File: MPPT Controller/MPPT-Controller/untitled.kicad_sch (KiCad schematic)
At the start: 29 parts, among them J5 USB_C_Receptacle_USB2.0_16P, U2 ESP32-WROOM-32D, U3 CH340C

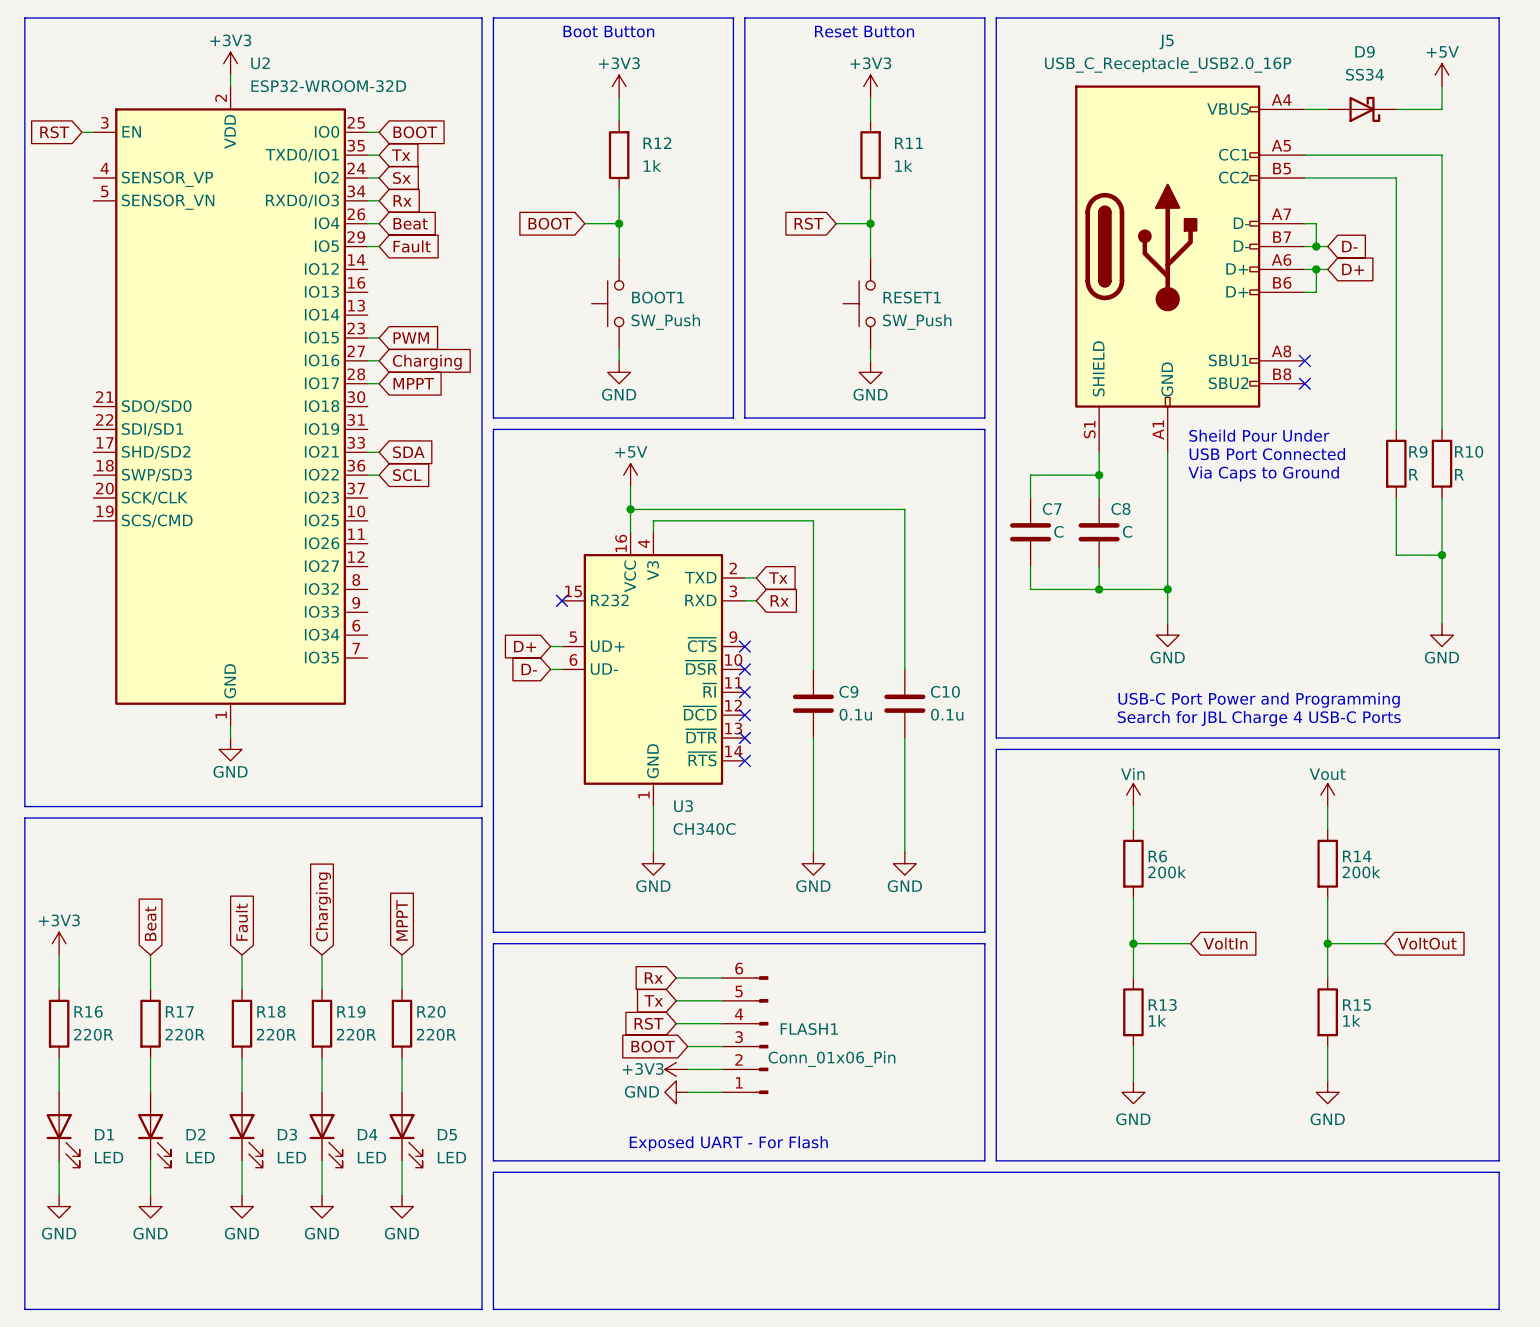
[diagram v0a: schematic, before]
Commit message: Add ADC Channels
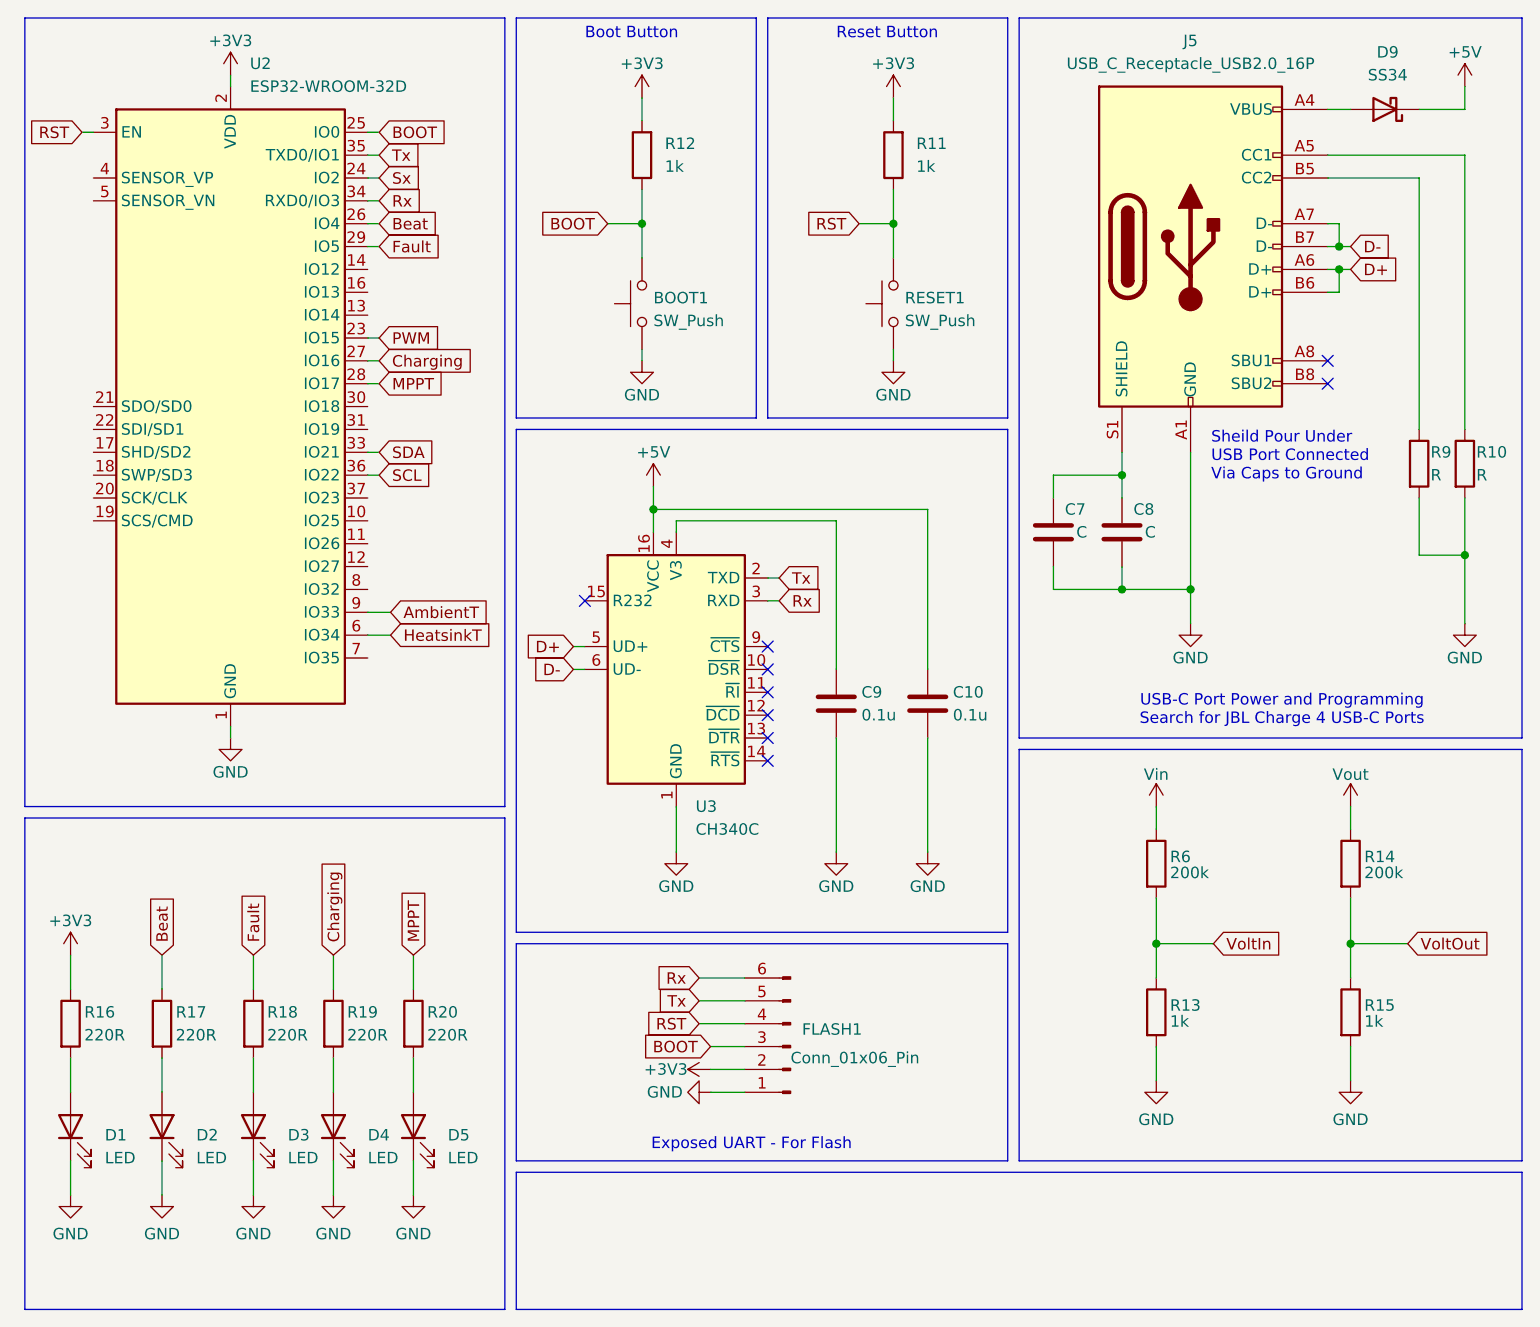
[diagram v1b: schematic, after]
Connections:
- net HeatsinkT: now reaches U2.6 (IO34)
- net AmbientT: now reaches U2.9 (IO33)
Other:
- moved on the sheet: BOOT1, C10, C7, C8, C9, D1, D2, D3, D4, D5, D9, FLASH1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

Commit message: Diode
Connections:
- net RDY1: now reaches U2.30 (IO18)
- net RDY2: now reaches U2.31 (IO19)
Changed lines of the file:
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@@
+	(wire
+		(pts
+			(xy 50.8 58.42) (xy 52.07 58.42)
+		)
+		(stroke
+			(width 0)
+			(type default)
+		)
+	)
 	(wire
 		(pts
@@
 	(wire
 		(pts
+			(xy 50.8 55.88) (xy 52.07 55.88)
+		)
+		(stroke
+			(width 0)
+			(type default)
+		)
+	)
+	(wire
+		(pts
 			(xy 38.1 139.7) (xy 38.1 143.51)
 		)
@@
 		)
 	)
+	(global_label "RDY1"
+		(shape input)
+		(at 52.07 55.88 0)
+		(fields_autoplaced yes)
+		(effects
+			(font
+				(size 1.27 1.27)
+			)
+			(justify left)
+		)
+		(property "Intersheetrefs" "${INTERSHEET_REFS}"
+			(at 59.8933 55.88 0)
+			(effects
+				(font
+					(size 1.27 1.27)
+				)
+				(justify left)
+				(hide yes)
+			)
+		)
+	)
 	(global_label "Rx"
 		(shape input)
@@
 			(effects
 				(font
+					(size 1.27 1.27)
+				)
+				(justify left)
+				(hide yes)
+			)
+		)
+	)
+	(global_label "RDY2"
+		(shape input)
+		(at 52.07 58.42 0)
+		(fields_autoplaced yes)
+		(effects
+			(font
+				(size 1.27 1.27)
+			)
+			(justify left)
+		)
+		(property "Intersheetrefs" "${INTERSHEET_REFS}"
+			(at 59.8933 58.42 0)
+			(effects
+				(font
